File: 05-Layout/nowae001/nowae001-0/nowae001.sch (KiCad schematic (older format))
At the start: 0 parts

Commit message: Added main circuit
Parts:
- added C?: 100nF, symbol CAPACITOR
- added C? (x2): 47pF, symbol CAPACITOR
- added DL?: GREEN, symbol GREEN
- added DL?: YELLOW, symbol YELLOW
- added R? (x2): 270, symbol RESISTOR
- added R? (x2): 27, symbol RESISTOR
- added U?: FT230XQ, QFN16, symbol FT230XQ
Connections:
- net labels added: EN_PWR, GND, VCCIO
- wire segments 0 -> 42

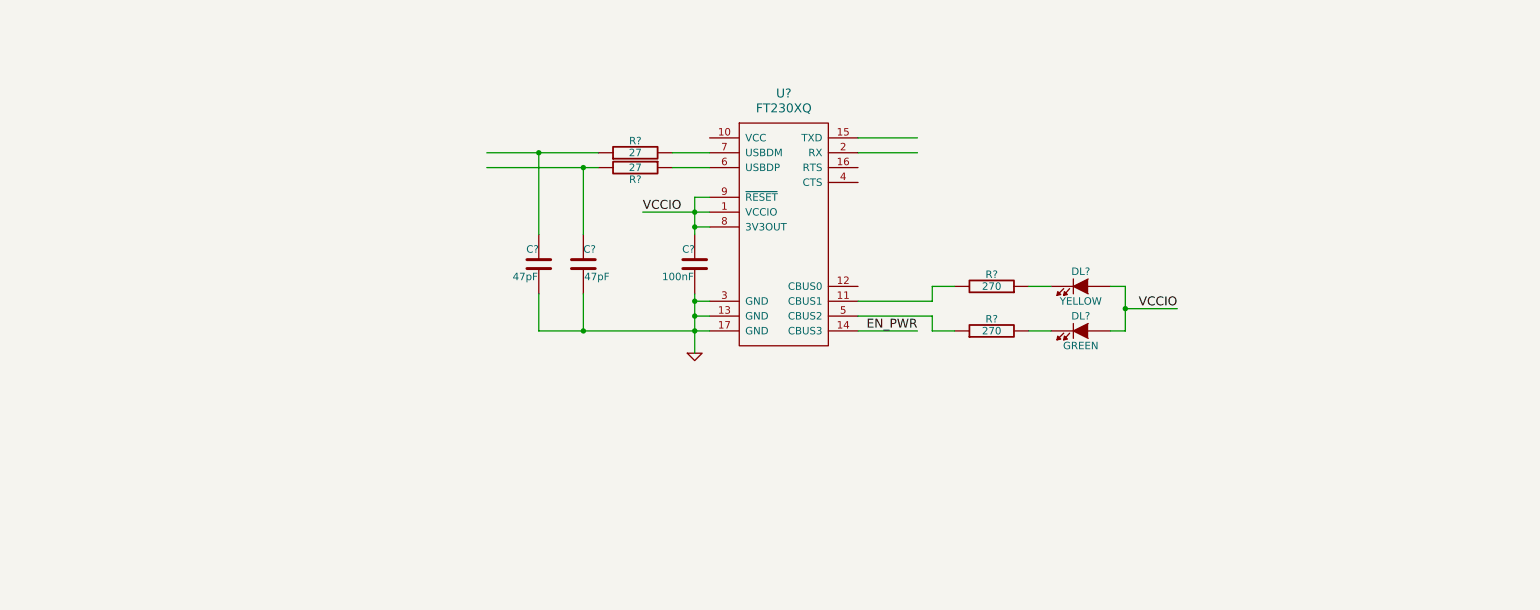
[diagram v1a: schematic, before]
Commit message: Added switching regulator +3.3V
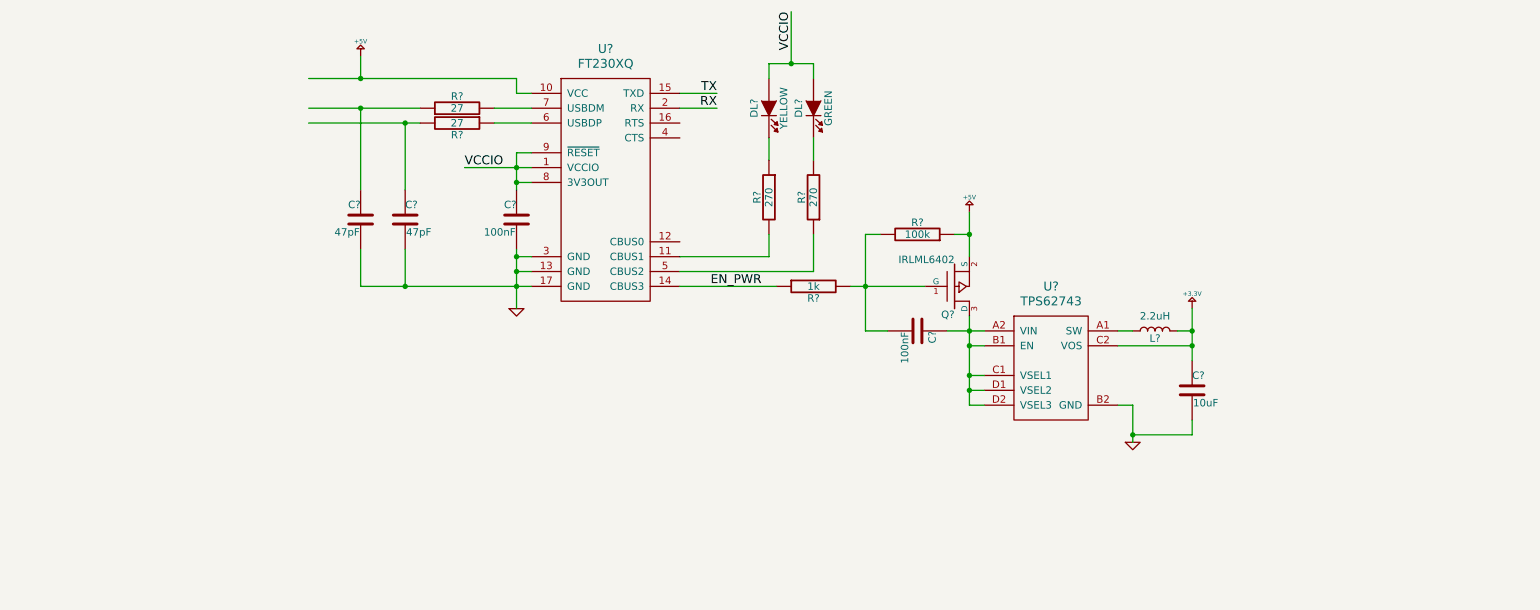
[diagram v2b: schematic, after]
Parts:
- added C?: 10uF, symbol CAPACITOR
- added C?: 100nF, symbol CAPACITOR
- added L?: 2.2uH, symbol INDUCTOR
- added Q?: IRLML6402, symbol IRLML6402
- added R?: 100k, symbol RESISTOR
- added R?: 1k, symbol RESISTOR
- added U?: TPS62743, DSBGA8, symbol TPS62743
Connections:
- net labels added: +3.3V, +5V, RX, TX
- wire segments 42 -> 76
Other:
- moved on the sheet: C?, DL?, R?, U?

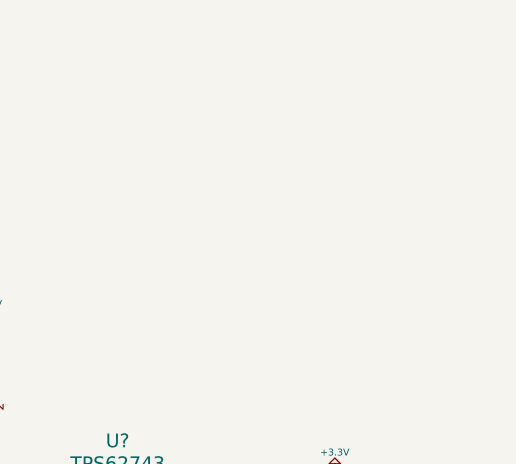
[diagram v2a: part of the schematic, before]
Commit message: Added UART output connector
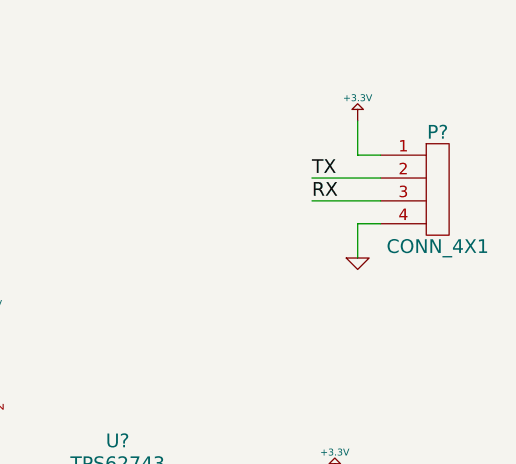
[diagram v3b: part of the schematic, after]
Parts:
- added P?: CONN_4X1, symbol CONN_4X1
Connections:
- wire segments 76 -> 82
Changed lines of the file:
@@
 Wire Wire Line
 	8450 5450 8450 5200
+$Comp
+L CONN_4X1 P?
+U 1 1 58A00615
+P 11450 4450
+F 0 "P?" H 11450 4700 60  0000 C CNN
+F 1 "CONN_4X1" H 11450 4200 60  0000 C CNN
+F 2 "" H 11825 4450 60  0000 C CNN
+F 3 "" H 11825 4450 60  0000 C CNN
+	1    11450 4450
+	1    0    0    -1
+$EndComp
+Wire Wire Line
+	11100 4300 11200 4300
+Wire Wire Line
+	11100 4150 11100 4300
+$Comp
+L +3.3V #PWR?
+U 1 1 58A00B9C
+P 11100 4150
+F 0 "#PWR?" H 11100 4075 30  0001 C CNN
+F 1 "+3.3V" H 11100 4250 30  0000 C CNN
+F 2 "" H 11100 4150 60  0000 C CNN
+F 3 "" H 11100 4150 60  0000 C CNN
+	1    11100 4150
+	1    0    0    -1
+$EndComp
+Wire Wire Line
+	11100 4600 11100 4750
+Wire Wire Line
+	11200 4600 11100 4600
+$Comp
+L GND #PWR?
+U 1 1 58A0095D
+P 11100 4750
+F 0 "#PWR?" H 11100 4750 30  0001 C CNN
+F 1 "GND" H 11100 4750 30  0001 C CNN
+F 2 "" H 11100 4750 60  0000 C CNN
+F 3 "" H 11100 4750 60  0000 C CNN
+	1    11100 4750
+	1    0    0    -1
+$EndComp
+Text Label 10900 4500 0    60   ~ 0
+RX
+Text Label 10900 4400 0    60   ~ 0
+TX
+Wire Wire Line
+	10900 4500 11200 4500
+Wire Wire Line
+	10900 4400 11200 4400
 $EndSCHEMATC

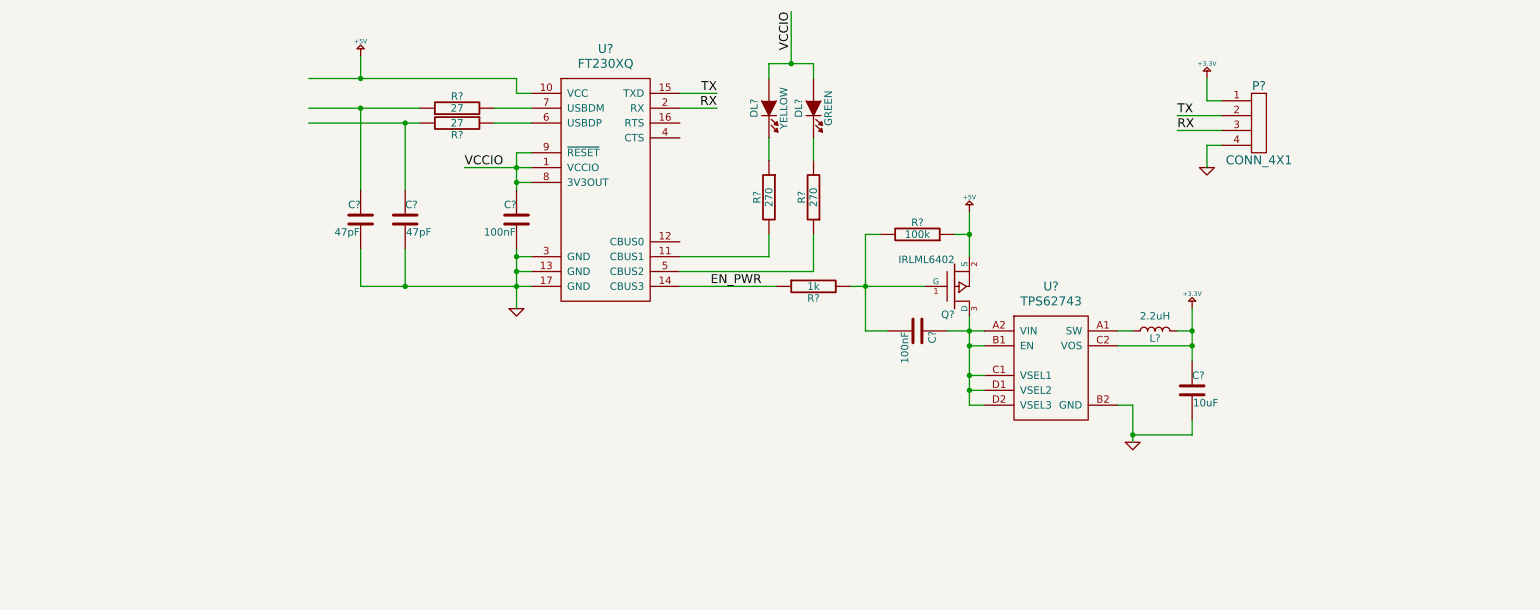
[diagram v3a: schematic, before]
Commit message: Added usb plug
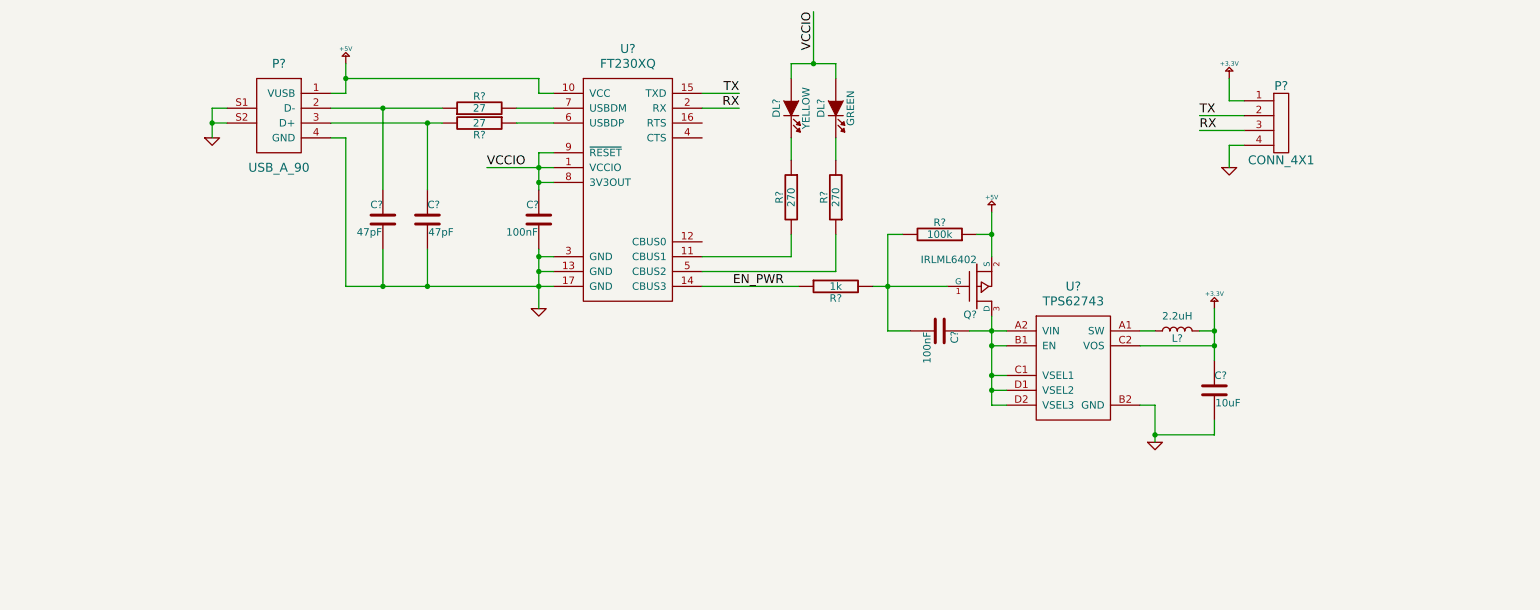
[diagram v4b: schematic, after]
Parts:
- added P?: USB_A_90, symbol USB_A_90
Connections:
- wire segments 82 -> 65
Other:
- moved on the sheet: C?, DL?, L?, P?, Q?, R?, U?

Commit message: Added led for power supply
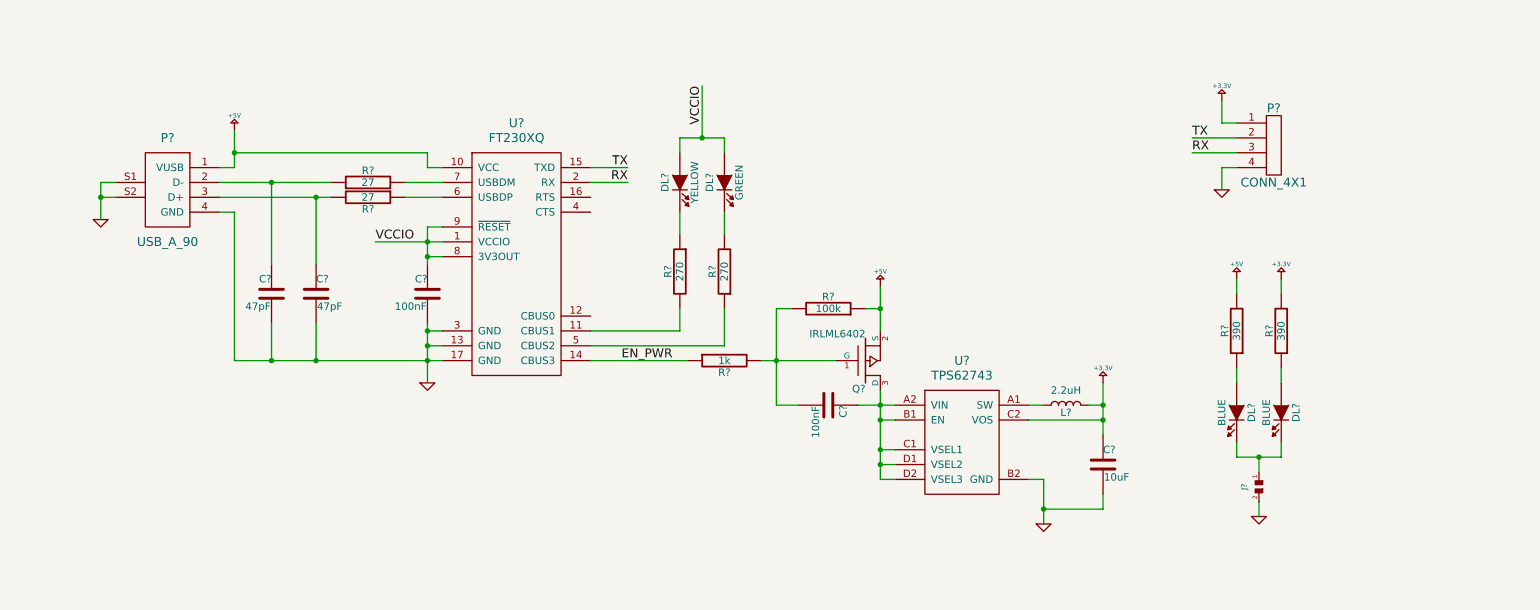
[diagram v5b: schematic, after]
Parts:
- added DL? (x2): BLUE, symbol BLUE
- added J?: SMALL_JUMPER, symbol SMALL_JUMPER
- added R? (x2): 390, symbol RESISTOR
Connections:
- net +3.3V: now also R?.2
- net +5V: now also R?.2
- net GND: now also J?.2
- new net: DL?.1 (A), R?.1 (x2)
- new net: DL?.2 (K), DL?.2 (K), J?.1
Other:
- moved on the sheet: C?, DL?, L?, P?, Q?, R?, U?

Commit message: Added Vin capacitor on TPS62743 and annotate components
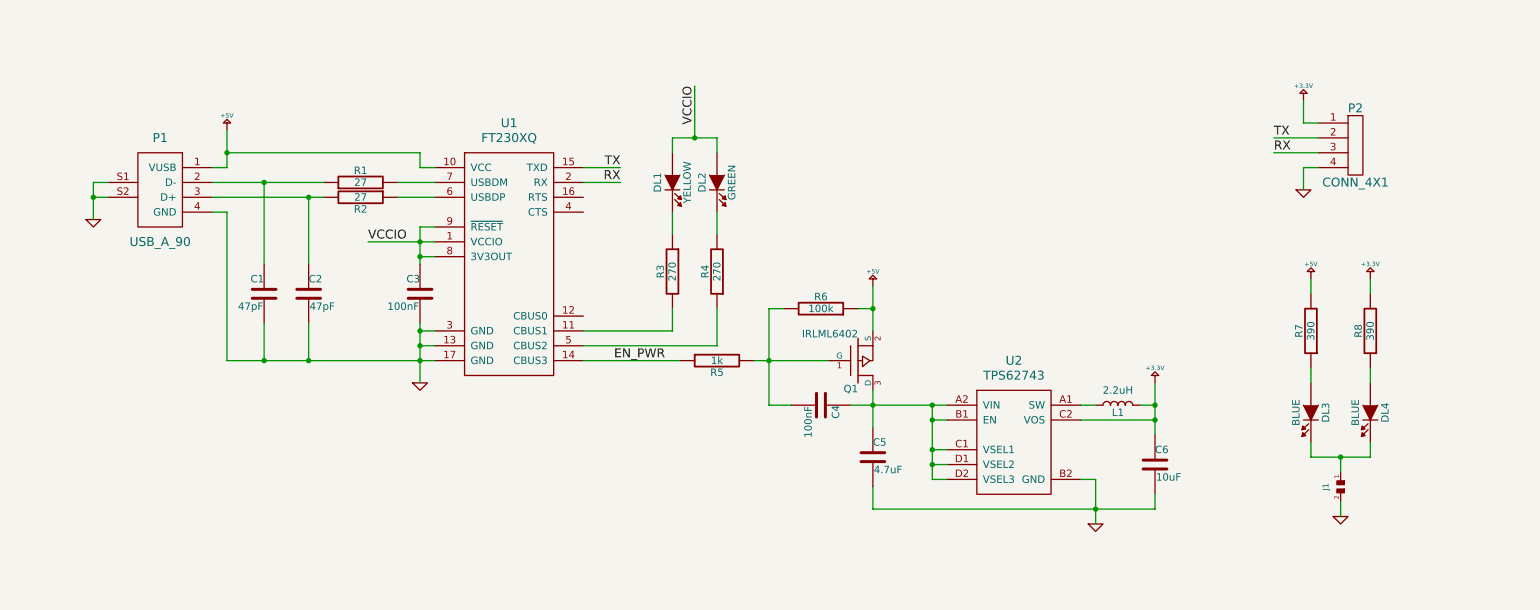
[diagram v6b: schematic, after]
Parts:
- added C5: 4.7uF, CAPACITOR:CAPACITOR-0402, symbol CAPACITOR
- C1, C2, C3, C4: renamed from C?; footprint (none) -> CAPACITOR:CAPACITOR-0402
- C6: renamed from C?; footprint (none) -> CAPACITOR:CAPACITOR-0603
- L1: renamed from L?; footprint (none) -> INDUCTOR:INDUCTOR-0805
- Q1: renamed from Q?; footprint (none) -> SOT:SOT23-3
- R1, R2, R3, R4, R5, R6, R7, R8: renamed from R?; footprint (none) -> RESISTOR:RESISTOR-0402
- U1: renamed from U?; footprint QFN16 -> QFN:QFN16_3x3_0.5
- U2: renamed from U?; footprint DSBGA8 -> BGA:DSBGA6_1.6X0.9_0.4
- gave numbers to parts that had none: 7
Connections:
- net GND: now also C5.2
- net at C4.1, Q1.3 (D), U2.A2 (VIN)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: now also C5.1
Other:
- moved on the sheet: C1, C2, C3, C4, C6, DL1, DL2, DL3, DL4, J1, L1, P1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

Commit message: Changed switching regulator (TPS62743 -> TPS62152) in nowae001
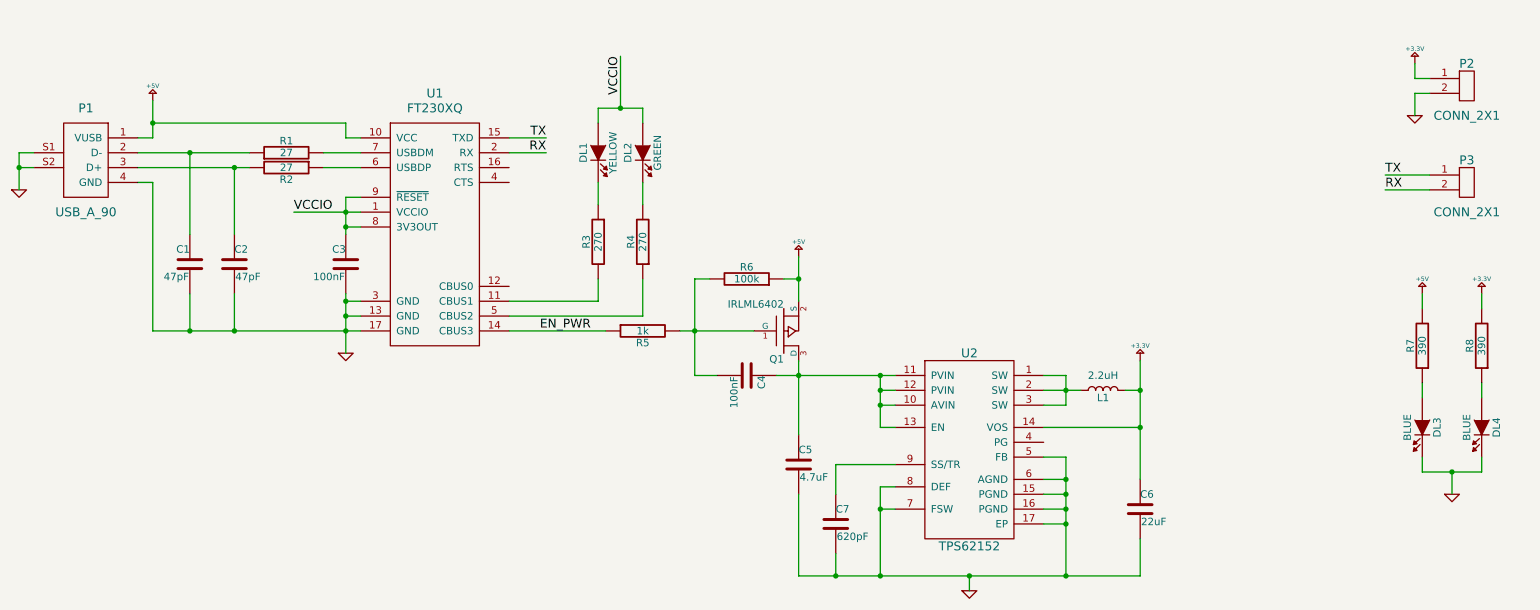
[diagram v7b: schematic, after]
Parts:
- removed J1: SMALL_JUMPER, symbol SMALL_JUMPER
- removed P2: CONN_4X1, symbol CONN_4X1
- removed U2: TPS62743, BGA:DSBGA6_1.6X0.9_0.4, symbol TPS62743
- added C7: 620pF, CAPACITOR:CAPACITOR-0402, symbol CAPACITOR
- added P2, P3: CONN_2X1, CONNECTOR_MKDS:CONN-MKDS1_2-3.81, symbol CONN_2X1
- added U2: TPS62152, QFN:QFN16_3x3_0.5_16+1, symbol TPS62152
- C6: value 10uF -> 22uF
- DL1, DL2, DL3, DL4: footprint (none) -> LEDs:LED-0402
- P1: footprint (none) -> CONNECTOR:USB-A-PLUG-SMD
- U1: footprint QFN:QFN16_3x3_0.5 -> QFN:QFN16_3x3_0.5_16+1
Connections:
- net +3.3V: now also P2.1, U2.14 (VOS)
- net GND: now also DL3.2 (K), DL4.2 (K), C7.2, P2.2, U2.15 (PGND), U2.16 (PGND), U2.17 (EP), U2.5 (FB), U2.6 (AGND), U2.7 (FSW), U2.8 (DEF)
- net RX: now also P3.2
- net TX: now also P3.1
- net at L1.1: now also U2.1 (SW), U2.2 (SW), U2.3 (SW)
- net at C4.1, C5.1, Q1.3 (D): now also U2.10 (AVIN), U2.11 (PVIN), U2.12 (PVIN), U2.13 (EN)
- new net: C7.1, U2.9 (SS/TR)
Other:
- moved on the sheet: C1, C2, C3, C4, C5, C6, DL1, DL2, DL3, DL4, L1, P1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

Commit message: Changed output connector in nowae001
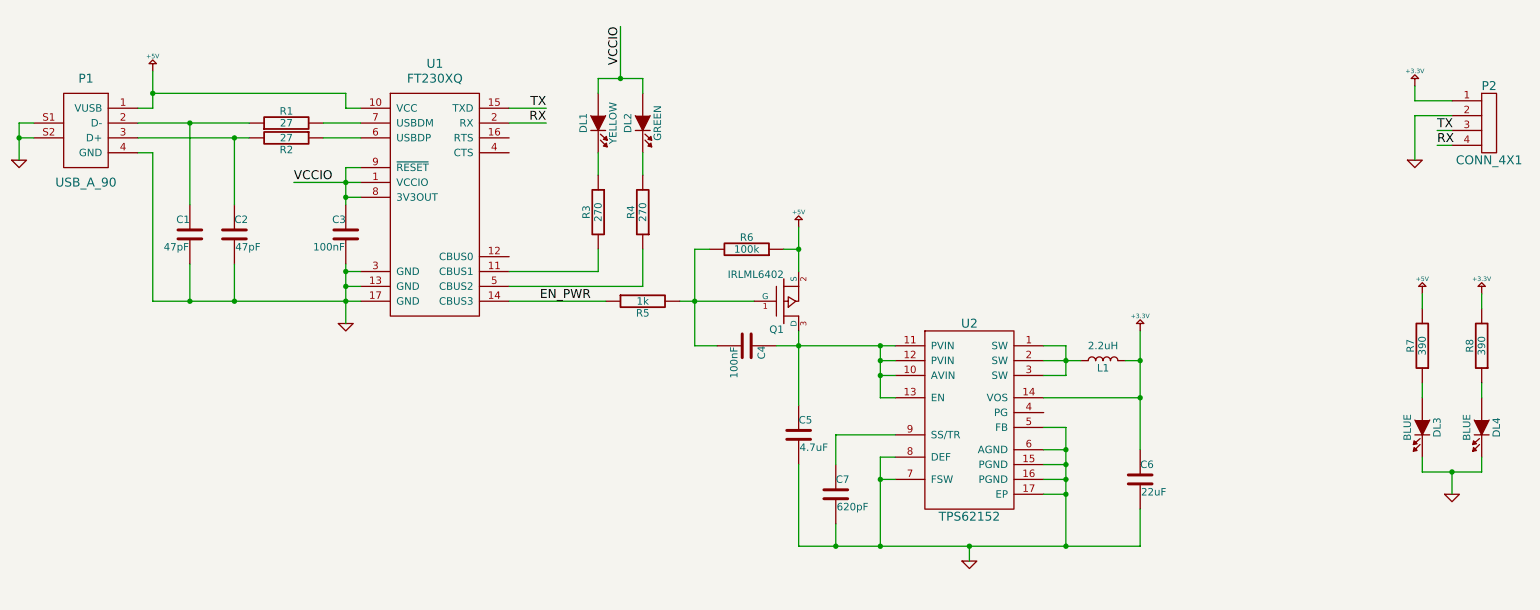
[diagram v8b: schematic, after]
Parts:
- removed P2, P3: CONN_2X1, CONNECTOR_MKDS:CONN-MKDS1_2-3.81, symbol CONN_2X1
- added P2: CONN_4X1, CONNECTOR_MKDS:CONN-MKDS1_4-3.81, symbol CONN_4X1
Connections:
- net +3.3V: now also P2.1
- net GND: now also P2.2
- net RX: now also P2.4
- net TX: now also P2.3
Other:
- moved on the sheet: C1, C2, C3, C4, C5, C6, C7, DL1, DL2, L1, P1, Q1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
